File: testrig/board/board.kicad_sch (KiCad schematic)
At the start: 15 parts, among them J1 Conn_01x20, J2 Conn_01x20, SW1 SW_DIP_x01, U1 AMS1117-3.3, U2 XO2-DIP20, U3 74HC574, U4 74HC574, U5 74HC574, U6 74HC574

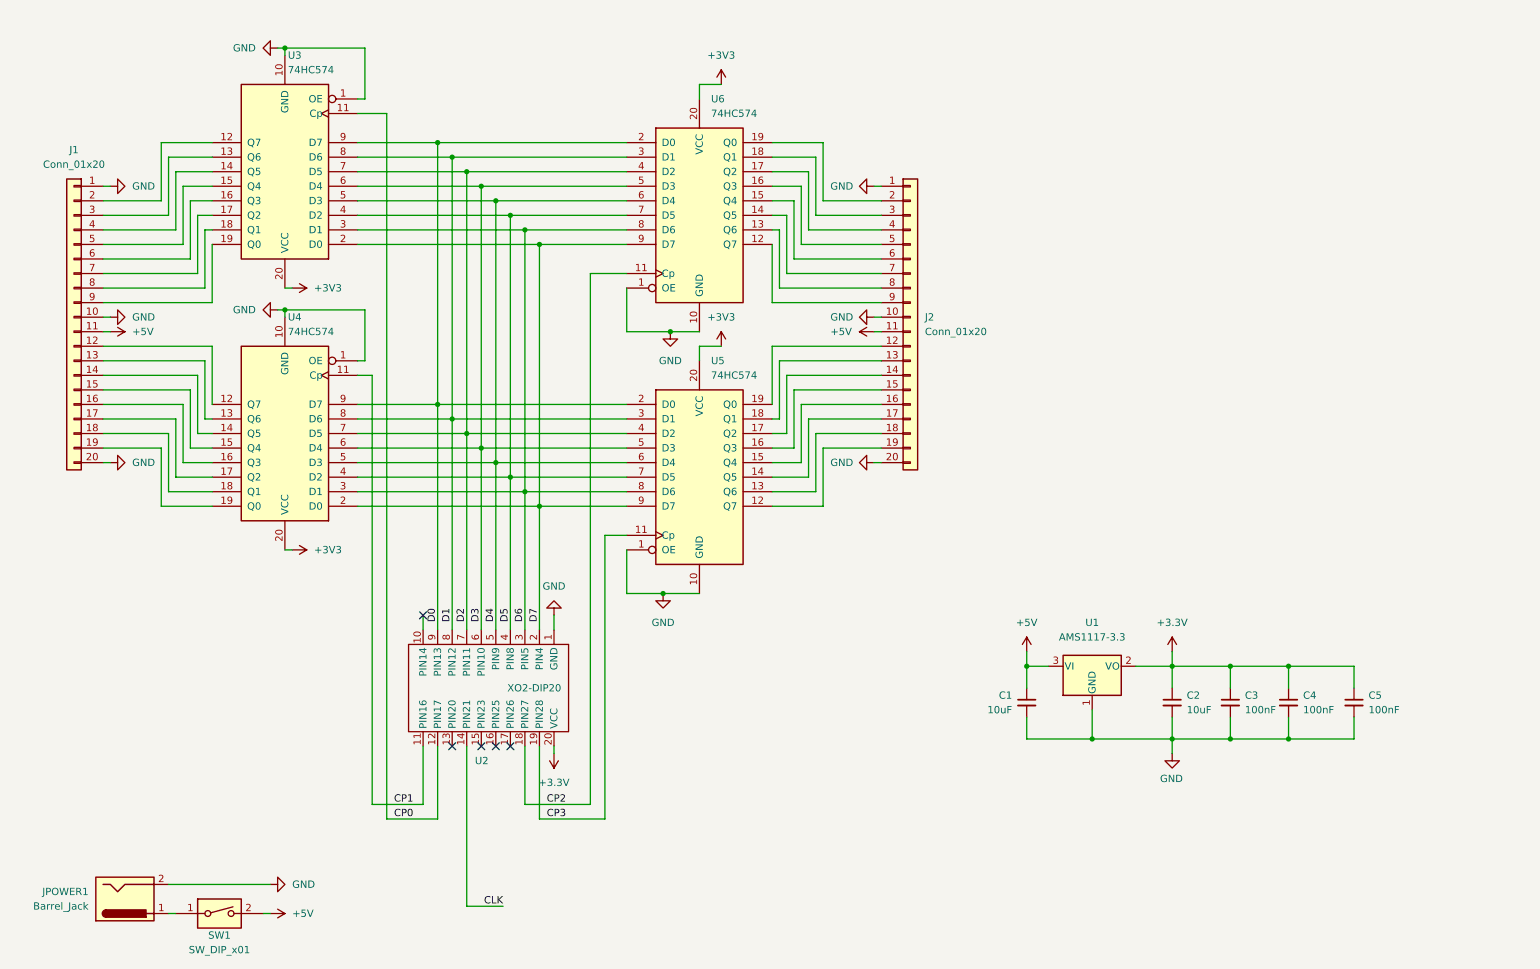
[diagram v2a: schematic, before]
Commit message: Digital test signals to drive the TIAdigitizer
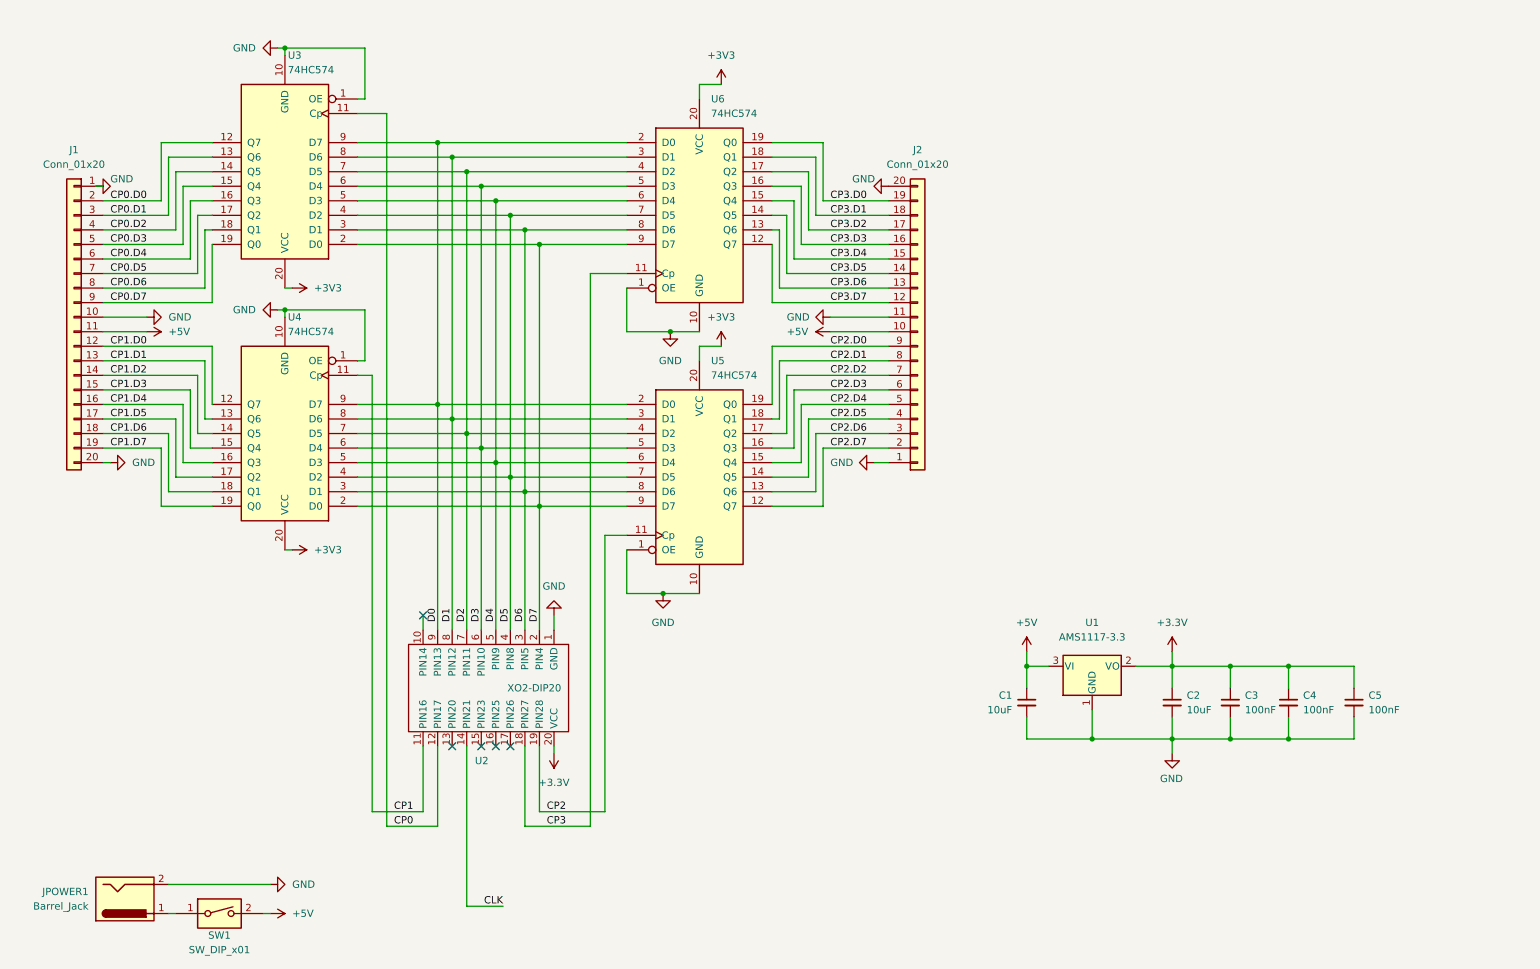
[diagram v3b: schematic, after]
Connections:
- net +5V: now also J2.10 (Pin_10); no longer J2.11 (Pin_11)
- net CP2: now also U2.19 (PIN28), U5.11 (Cp); no longer U2.18 (PIN27), U6.11 (Cp)
- net CP3: now also U2.18 (PIN27), U6.11 (Cp); no longer U2.19 (PIN28), U5.11 (Cp)
- net GND: now also J2.11 (Pin_11); no longer J2.10 (Pin_10)
- net CP0.D0: now reaches J1.2 (Pin_2), U3.12 (Q7)
- net CP0.D1: now reaches J1.3 (Pin_3), U3.13 (Q6)
- net CP0.D2: now reaches J1.4 (Pin_4), U3.14 (Q5)
- net CP0.D3: now reaches J1.5 (Pin_5), U3.15 (Q4)
- net CP0.D4: now reaches J1.6 (Pin_6), U3.16 (Q3)
- net CP0.D5: now reaches J1.7 (Pin_7), U3.17 (Q2)
- net CP0.D6: now reaches J1.8 (Pin_8), U3.18 (Q1)
- net CP0.D7: now reaches J1.9 (Pin_9), U3.19 (Q0)
- net CP2.D7: now reaches U5.12 (Q7)
- net CP2.D7: now also J2.2 (Pin_2); no longer J2.19 (Pin_19)
- net CP2.D6: now reaches U5.13 (Q6)
- net CP2.D6: now also J2.3 (Pin_3); no longer J2.18 (Pin_18)
- net CP2.D5: now reaches U5.14 (Q5)
- net CP2.D5: now also J2.4 (Pin_4); no longer J2.17 (Pin_17)
- net CP2.D4: now reaches U5.15 (Q4)
- net CP2.D4: now also J2.5 (Pin_5); no longer J2.16 (Pin_16)
- net CP2.D3: now reaches U5.16 (Q3)
- net CP2.D3: now also J2.6 (Pin_6); no longer J2.15 (Pin_15)
- net CP2.D2: now reaches U5.17 (Q2)
- net CP2.D2: now also J2.7 (Pin_7); no longer J2.14 (Pin_14)
- net CP2.D1: now reaches U5.18 (Q1)
- net CP2.D1: now also J2.8 (Pin_8); no longer J2.13 (Pin_13)
- net CP2.D0: now reaches U5.19 (Q0)
- net CP2.D0: now also J2.9 (Pin_9); no longer J2.12 (Pin_12)
- net CP3.D0: now reaches U6.19 (Q0)
- net CP3.D0: now also J2.19 (Pin_19); no longer J2.2 (Pin_2)
- net CP3.D1: now reaches U6.18 (Q1)
- net CP3.D1: now also J2.18 (Pin_18); no longer J2.3 (Pin_3)
- net CP3.D2: now reaches U6.17 (Q2)
- net CP3.D2: now also J2.17 (Pin_17); no longer J2.4 (Pin_4)
- net CP3.D3: now reaches U6.16 (Q3)
- net CP3.D3: now also J2.16 (Pin_16); no longer J2.5 (Pin_5)
- net CP3.D4: now reaches U6.15 (Q4)
- net CP3.D4: now also J2.15 (Pin_15); no longer J2.6 (Pin_6)
- net CP3.D5: now reaches U6.14 (Q5)
- net CP3.D5: now also J2.14 (Pin_14); no longer J2.7 (Pin_7)
- net CP3.D6: now reaches U6.13 (Q6)
- net CP3.D6: now also J2.13 (Pin_13); no longer J2.8 (Pin_8)
- net CP3.D7: now reaches U6.12 (Q7)
- net CP3.D7: now also J2.12 (Pin_12); no longer J2.9 (Pin_9)
- net CP1.D0: now reaches J1.12 (Pin_12), U4.12 (Q7)
- net CP1.D1: now reaches J1.13 (Pin_13), U4.13 (Q6)
- net CP1.D2: now reaches J1.14 (Pin_14), U4.14 (Q5)
- net CP1.D3: now reaches J1.15 (Pin_15), U4.15 (Q4)
- net CP1.D4: now reaches J1.16 (Pin_16), U4.16 (Q3)
- net CP1.D5: now reaches J1.17 (Pin_17), U4.17 (Q2)
- net CP1.D6: now reaches J1.18 (Pin_18), U4.18 (Q1)
- net CP1.D7: now reaches J1.19 (Pin_19), U4.19 (Q0)
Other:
- moved on the sheet: J2

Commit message: Add direct output pin for fast path
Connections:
- net GND: no longer J1.10 (Pin_10)
- net DIRECT: now reaches U2.10 (PIN14)
- net DIRECT: now also J1.10 (Pin_10)
- no-connect marks 5 -> 4

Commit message: Add mode switch
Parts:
- added R1: 10k, symbol Device:R_Small
- added SW2: SW_DIP_x01, symbol Switch:SW_DIP_x01
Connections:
- net +3.3V: now also R1.1
- net GND: now also SW2.2
- net at U2.17 (PIN26): now also R1.2, SW2.1
- no-connect marks 4 -> 3
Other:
- note added: "25MHz"
- note added: "MODE"
